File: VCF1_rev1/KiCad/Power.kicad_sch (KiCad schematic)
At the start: 10 parts, among them U3 CEM3350, U7 Opamp_Quad, U9 LM13700

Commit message: Added VCA (with a quirk) and also drew a new symbol for 74HC4053 because the standard one annoyed me.
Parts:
- gave numbers to parts that had none: 3
- renumbered C22 to C21, C23 to C22, C24 to C23, C25 to C24

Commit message: The filter blocks are more or less done, page order has gotten more sane for easier reading.
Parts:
- added C19, C20, C25, C26: 100nF, symbol Device:C
- added U15: CEM3350, symbol Modular_Mayhem:CEM3350
- added U4: Opamp_Quad, symbol Device:Opamp_Quad
- renumbered C19 to C21, C20 to C22, C21 to C23, C22 to C24, C23 to C27, C24 to C28, U7 to U1, U8 to U11, U9 to U19, U3 to U6
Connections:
- net +10V: now also C19.1, C25.1, U15.16 (Vcc), U4.4 (V+)
- net -10V: now also C20.2, C26.2, U15.7 (Vee), U4.11 (V-)
- net GND: now also C19.2, C20.1, C25.2, C26.1, U15.9 (GND)
- net VCF_Iref: now also U15.1 (Iref)

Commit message: Lot of work on panel etc.
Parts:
- renumbered C19 to C18, C20 to C19, C21 to C20, C22 to C21, C23 to C22, C24 to C23, C25 to C24, C26 to C25, C27 to C26, C28 to C27, U6 to U10, U11 to U14, U15 to U16, U19 to U5

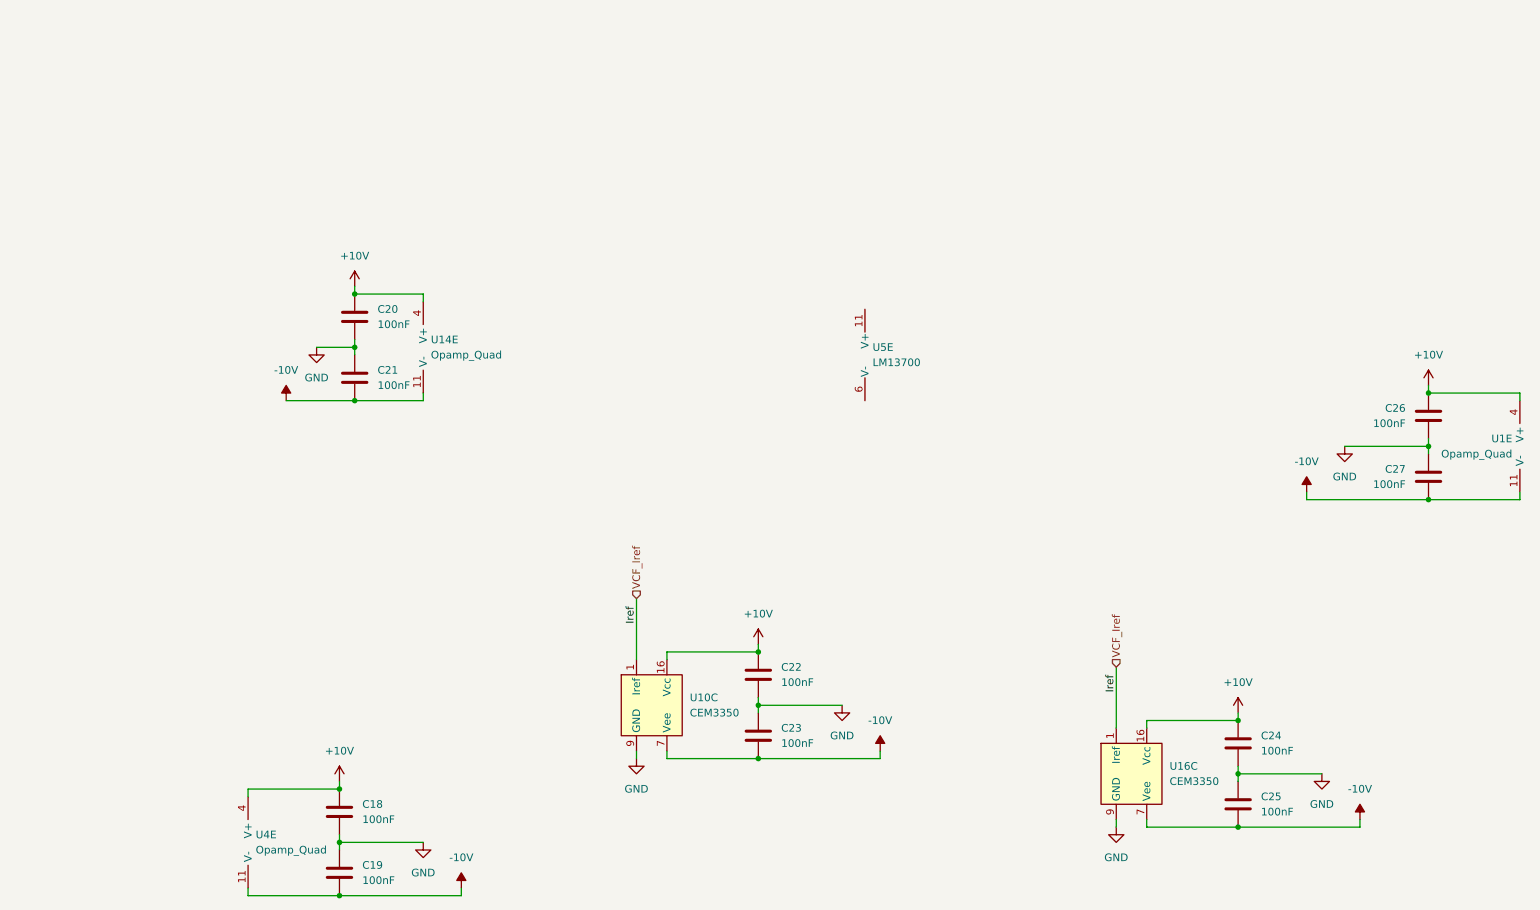
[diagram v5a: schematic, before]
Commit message: Cleaned up the first page with the overview and tried to make it a bit more readable.
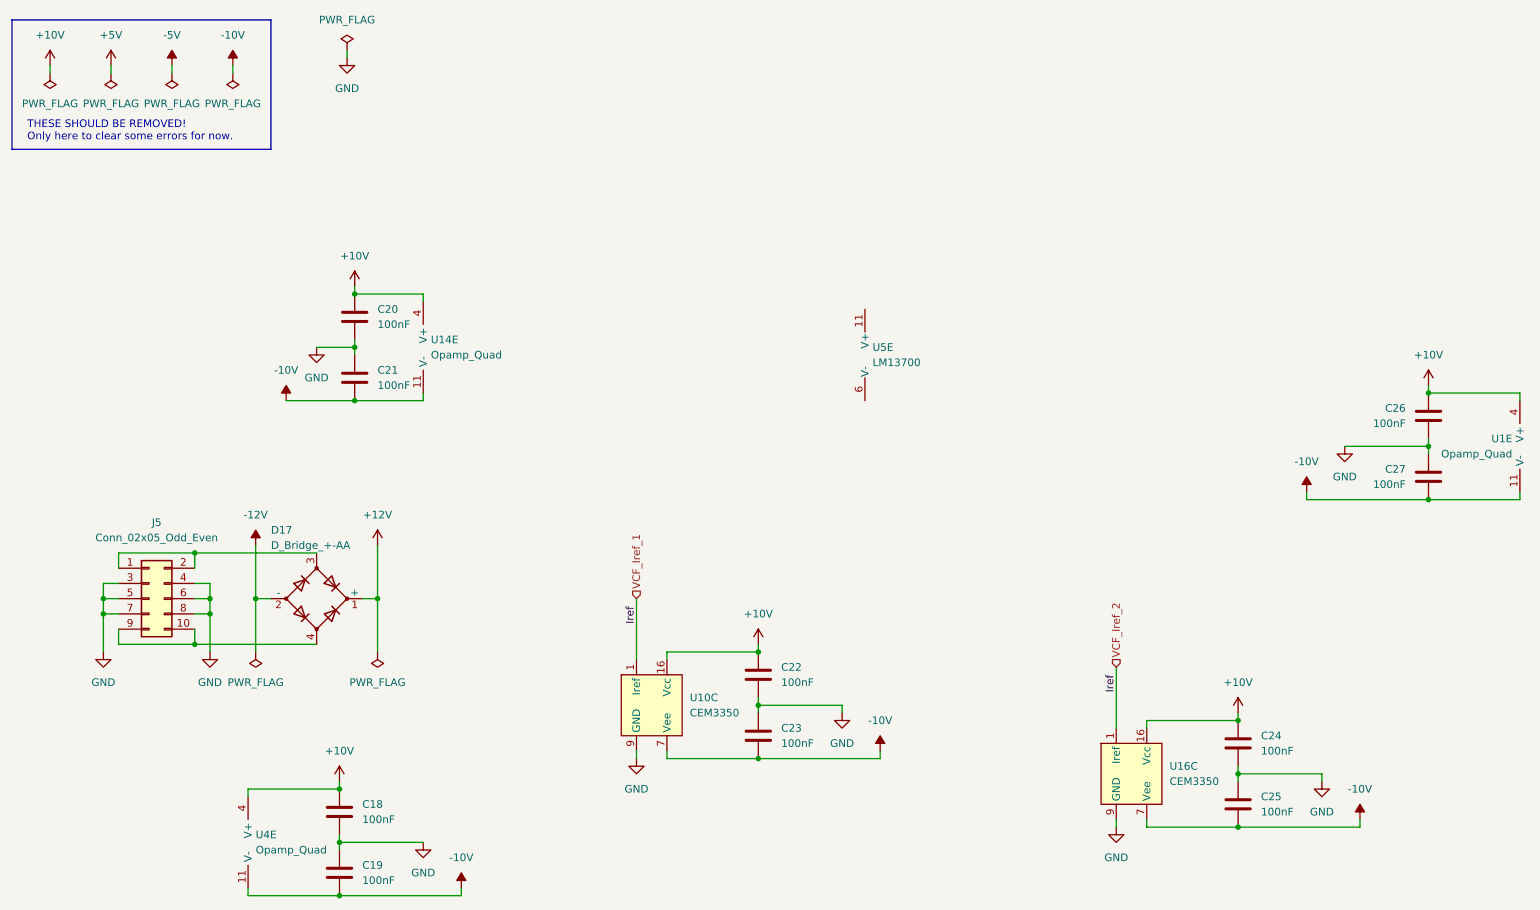
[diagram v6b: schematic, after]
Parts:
- added D17: D_Bridge_+-AA, symbol Device:D_Bridge_+-AA
- added J5: Conn_02x05_Odd_Even, symbol Connector_Generic:Conn_02x05_Odd_Even
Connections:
- net GND: now also J5.3 (Pin_3), J5.4 (Pin_4), J5.5 (Pin_5), J5.6 (Pin_6), J5.7 (Pin_7), J5.8 (Pin_8)
- net VCF_Iref renamed VCF_Iref_1
- new net: D17.3, J5.1 (Pin_1), J5.2 (Pin_2)
- new net: D17.4, J5.10 (Pin_10), J5.9 (Pin_9)
- new net +12V: D17.1 (+)
- new net -12V: D17.2 (-)
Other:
- note added: "THESE SHOULD BE REMOVED! Only here to clear some errors for now."

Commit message: Drew a better symbol for LM13700 because the other one was ugly.
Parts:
- removed U5: LM13700, symbol Amplifier_Operational:LM13700
- added U5: LM13700, symbol Modular_Mayhem:LM13700
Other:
- moved on the sheet: D17
